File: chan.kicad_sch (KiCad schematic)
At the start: 8 parts, among them J5 0836149012, J6 61083-061402LF, J7 61083-061402LF

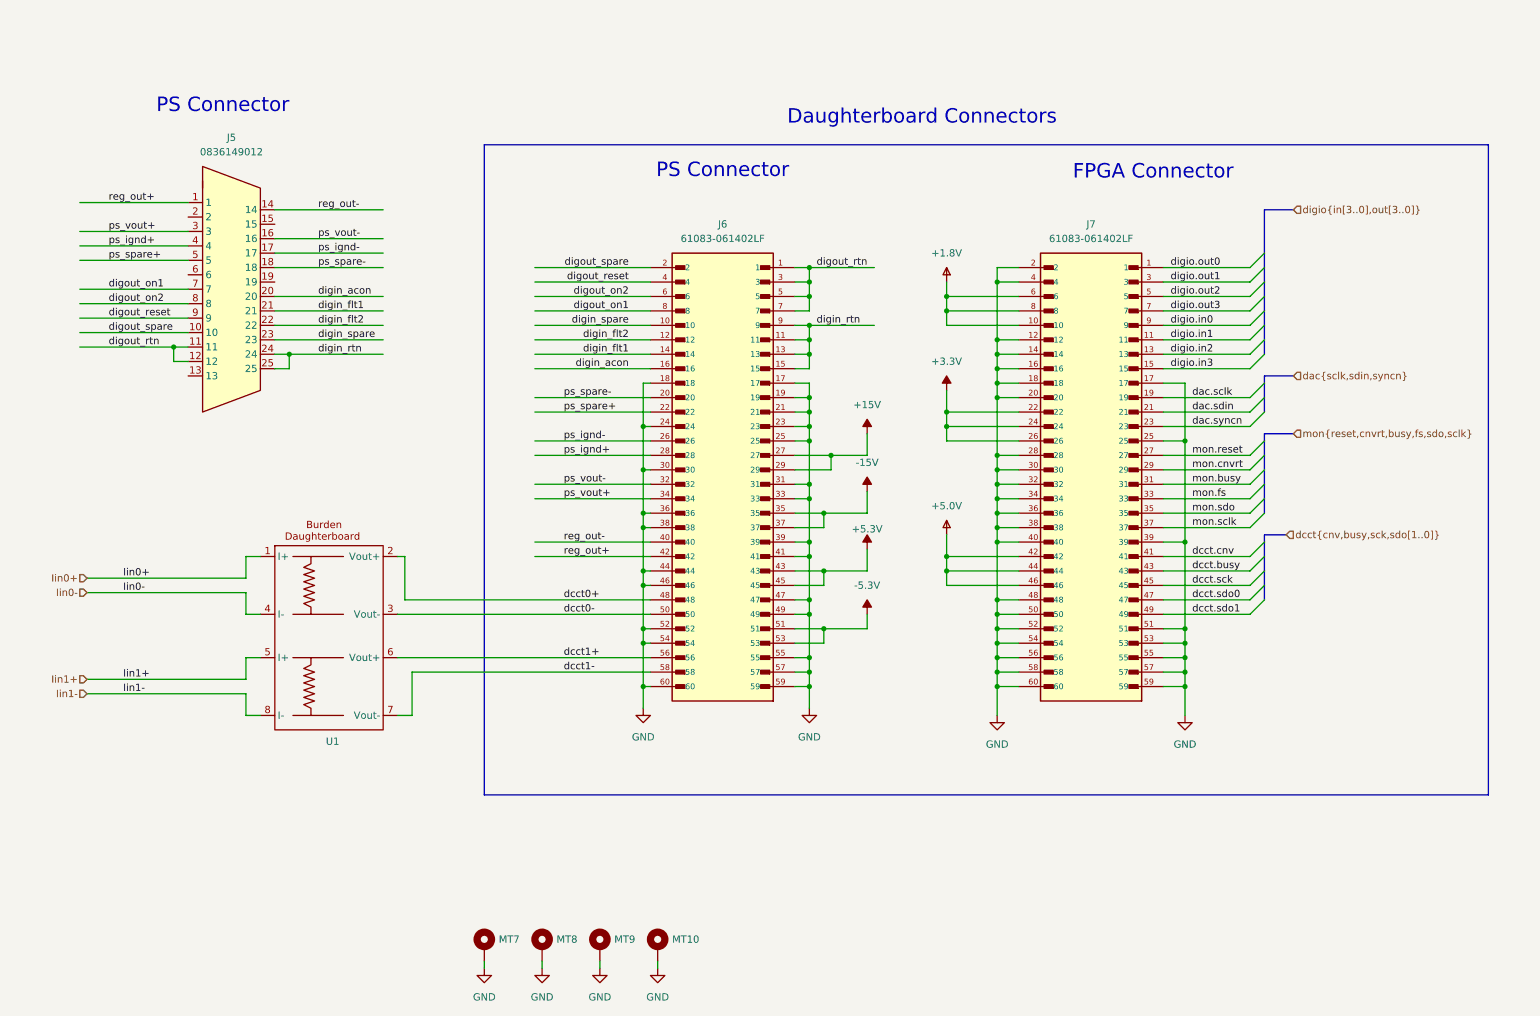
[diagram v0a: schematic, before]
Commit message: Add all 4 channels
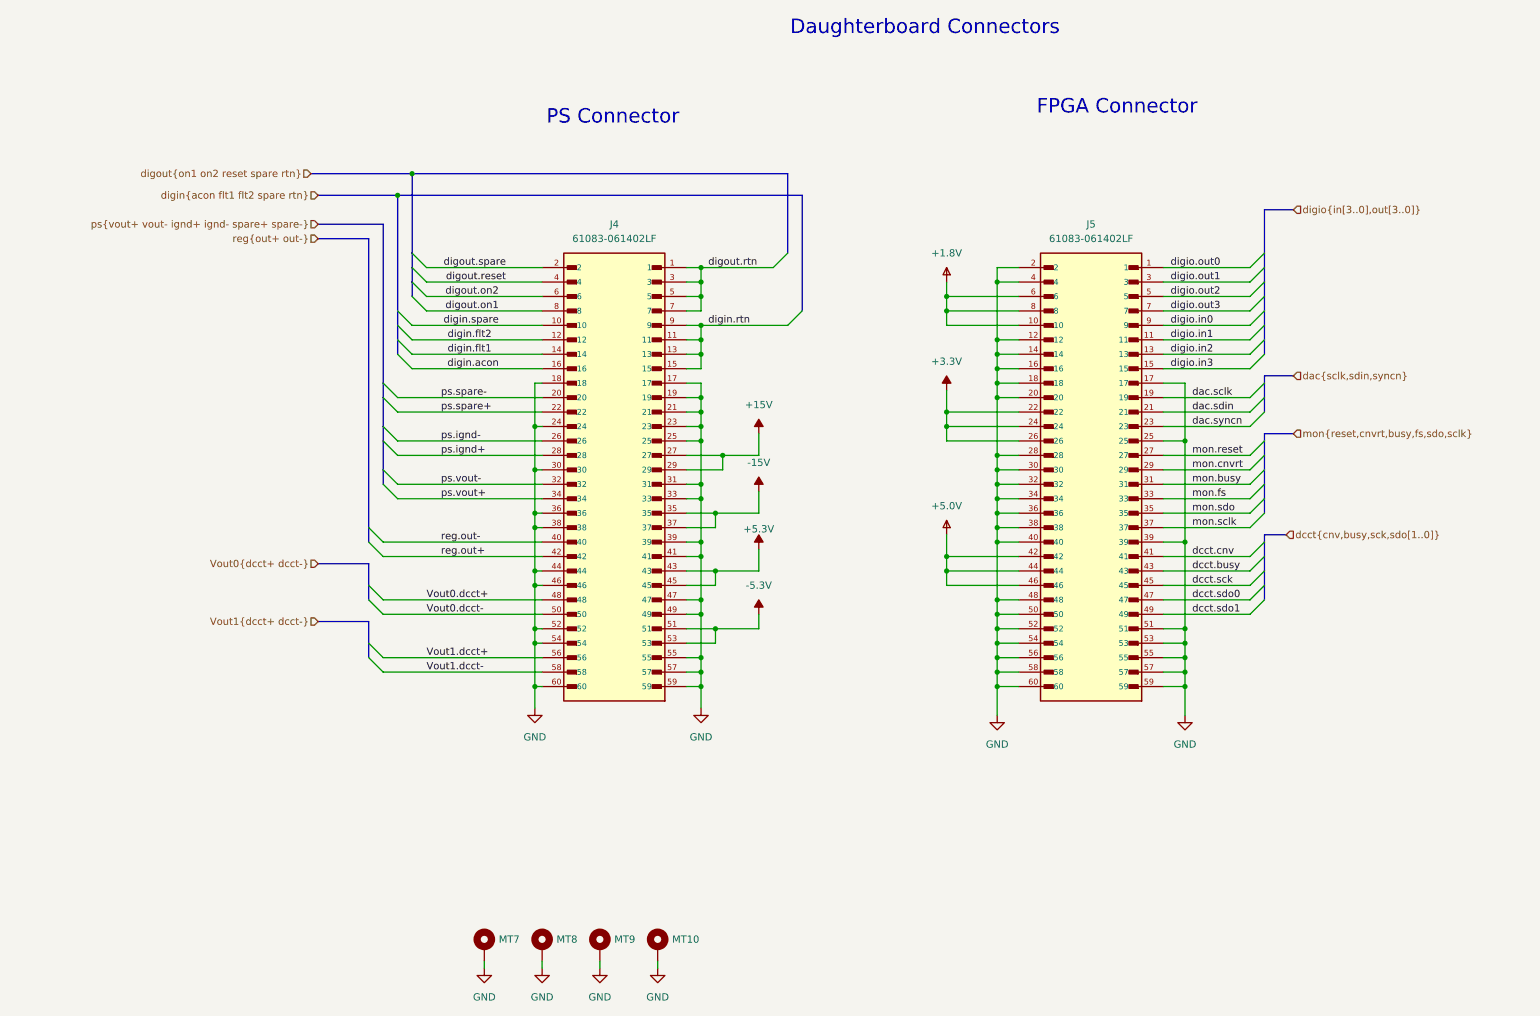
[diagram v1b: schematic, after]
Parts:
- removed J5: 0836149012, myparts:0836149012, symbol 0836149012:0836149012
- removed U1: ~, myparts:burden, symbol psc:burden
- renumbered J6 to J4, J7 to J5
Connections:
- net dcct0+ renamed Vout0.dcct+
- net dcct0- renamed Vout0.dcct-
- net dcct1+ renamed Vout1.dcct+
- net dcct1- renamed Vout1.dcct-
- net digin_acon renamed digin.acon
- net digin_flt1 renamed digin.flt1
- net digin_flt2 renamed digin.flt2
- net digin_rtn renamed digin.rtn
- net digin_spare renamed digin.spare
- net digout_on1 renamed digout.on1
- net digout_on2 renamed digout.on2
- net digout_reset renamed digout.reset
- net digout_rtn renamed digout.rtn
- net digout_spare renamed digout.spare
- net ps_ignd+ renamed ps.ignd+
- net ps_ignd- renamed ps.ignd-
- net ps_spare+ renamed ps.spare+
- net ps_spare- renamed ps.spare-
- net ps_vout+ renamed ps.vout+
- net ps_vout- renamed ps.vout-
- net reg_out+ renamed reg.out+
- net reg_out- renamed reg.out-
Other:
- moved on the sheet: J4

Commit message: Start routing
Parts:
- renumbered J4 to J5, J5 to J6
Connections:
- net digin.rtn: now also J5.1, J5.3, J5.5, J5.7; no longer J5.11, J5.13, J5.15, J5.9
- net digout.rtn: now also J5.11, J5.13, J5.15, J5.9; no longer J5.1, J5.3, J5.5, J5.7

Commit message: Finished layout
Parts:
- J5, J6: Cost (none) -> 2.81; MFG (none) -> Amphenol; MFG_PN (none) -> 61083-061402LF
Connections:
- net GND: no longer J6.56, J6.58, J6.60
- new net +2.5V: J6.56, J6.58, J6.60
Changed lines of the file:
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@@
 	)
 	(junction
-		(at 179.07 86.36)
+		(at 179.07 132.08)
 		(diameter 0)
 		(color 0 0 0 0)
 	)
 	(junction
-		(at 179.07 111.76)
+		(at 179.07 86.36)
 		(diameter 0)
 		(color 0 0 0 0)
 	)
 	(junction
-		(at 220.98 109.22)
+		(at 179.07 111.76)
 		(diameter 0)
 		(color 0 0 0 0)
 	)
 	(junction
-		(at 187.96 127)
+		(at 220.98 109.22)
 		(diameter 0)
 		(color 0 0 0 0)
 	)
 	(junction
-		(at 187.96 132.08)
+		(at 187.96 127)
 		(diameter 0)
 		(color 0 0 0 0)
@@
 	)
 	(junction
-		(at 187.96 134.62)
-		(diameter 0)
-		(color 0 0 0 0)
-	)
-	(junction
 		(at 179.07 68.58)
 		(diameter 0)
@@
 	)
 	(junction
-		(at 187.96 129.54)
-		(diameter 0)
-		(color 0 0 0 0)
-	)
-	(junction
 		(at 138.43 104.14)
 		(diameter 0)
@@
 	)
 	(junction
+		(at 179.07 129.54)
+		(diameter 0)
+		(color 0 0 0 0)
+	)
+	(junction
 		(at 135.89 66.04)
 		(diameter 0)
@@
 	(wire
 		(pts
+			(xy 179.07 129.54) (xy 179.07 127)
+		)
+		(stroke
+			(width 0)
+			(type default)
+		)
+	)
+	(wire
+		(pts
 			(xy 135.89 88.9) (xy 135.89 91.44)
 		)
@@
 	(wire
 		(pts
-			(xy 187.96 134.62) (xy 187.96 139.7)
+			(xy 187.96 127) (xy 187.96 139.7)
 		)
 		(stroke
@@
 	(wire
 		(pts
-			(xy 187.96 129.54) (xy 187.96 132.08)
-		)
-		(stroke
-			(width 0)
-			(type default)
-		)
-	)
-	(wire
-		(pts
 			(xy 133.35 91.44) (xy 135.89 91.44)
 		)
@@
 		)
 	)
-	(wire
-		(pts
-			(xy 191.77 134.62) (xy 187.96 134.62)
-		)
-		(stroke
-			(width 0)
-			(type default)
-		)
-	)
 	(bus
 		(pts
@@
 	(wire
 		(pts
-			(xy 191.77 129.54) (xy 187.96 129.54)
-		)
-		(stroke
-			(width 0)
-			(type default)
-		)
-	)
-	(wire
-		(pts
 			(xy 187.96 93.98) (xy 187.96 96.52)
 		)
@@
 		)
 	)
-	(wire
-		(pts
-			(xy 191.77 132.08) (xy 187.96 132.08)
-		)
-		(stroke
-			(width 0)
-			(type default)
-		)
-	)
 	(bus
 		(pts
@@
 	(wire
 		(pts
+			(xy 191.77 129.54) (xy 179.07 129.54)
+		)
+		(stroke
+			(width 0)
+			(type default)
+		)
+	)
+	(wire
+		(pts
 			(xy 97.79 184.15) (xy 97.79 182.88)
 		)
@@
 	(wire
 		(pts
-			(xy 187.96 132.08) (xy 187.96 134.62)
-		)
-		(stroke
-			(width 0)
-			(type default)
-		)
-	)
-	(wire
-		(pts
 			(xy 133.35 99.06) (xy 135.89 99.06)
 		)
@@
 		)
 	)
+	(wire
+		(pts
+			(xy 179.07 134.62) (xy 179.07 132.08)
+		)
+		(stroke
+			(width 0)
+			(type default)
+		)
+	)
 	(bus
 		(pts
@@
 	(wire
 		(pts
+			(xy 179.07 132.08) (xy 179.07 129.54)
+		)
+		(stroke
+			(width 0)
+			(type default)
+		)
+	)
+	(wire
+		(pts
 			(xy 191.77 119.38) (xy 187.96 119.38)
 		)
@@
 	(wire
 		(pts
+			(xy 191.77 132.08) (xy 179.07 132.08)
+		)
+		(stroke
+			(width 0)
+			(type default)
+		)
+	)
+	(wire
+		(pts
 			(xy 179.07 63.5) (xy 179.07 66.04)
 		)
@@
 	(wire
 		(pts
-			(xy 106.68 124.46) (xy 106.68 127)
+			(xy 191.77 134.62) (xy 179.07 134.62)
 		)
 		(stroke
@@
 	(wire
 		(pts
-			(xy 191.77 121.92) (xy 187.96 121.92)
+			(xy 106.68 124.46) (xy 106.68 127)
 		)
 		(stroke
@@
 	(wire
 		(pts
-			(xy 191.77 66.04) (xy 179.07 66.04)
+			(xy 191.77 121.92) (xy 187.96 121.92)
 		)
 		(stroke
@@
 	(wire
 		(pts
-			(xy 135.89 101.6) (xy 135.89 109.22)
+			(xy 191.77 66.04) (xy 179.07 66.04)
 		)
 		(stroke
@@
 	(wire
 		(pts
-			(xy 133.35 119.38) (xy 135.89 119.38)
+			(xy 135.89 101.6) (xy 135.89 109.22)
 		)
 		(stroke
@@
 	(wire
 		(pts
-			(xy 187.96 127) (xy 187.96 129.54)
+			(xy 133.35 119.38) (xy 135.89 119.38)
 		)
 		(stroke
@@
 	)
 	(symbol
+		(lib_id "psc:+2.5V")
+		(at 179.07 127 0)
+		(unit 1)
+		(exclude_from_sim no)
+		(in_bom yes)
+		(on_board yes)
+		(dnp no)
+		(fields_autoplaced yes)
+		(property "Reference" "#PWR0232"
+			(at 179.07 130.81 0)
+			(effects
+				(font
+					(size 1.27 1.27)
+				)
+				(hide yes)
+			)
+		)
+		(property "Value" "+2.5V"
+			(at 179.07 121.92 0)
+			(effects
+				(font
+					(size 1.27 1.27)
+				)
+			)
+		)
+		(property "Footprint" ""
+			(at 179.07 127 0)
+			(effects
+				(font
+					(size 1.27 1.27)
+				)
+				(hide yes)
+			)
+		)
+		(property "Datasheet" ""
+			(at 179.07 127 0)
+			(effects
+				(font
+					(size 1.27 1.27)
+				)
+				(hide yes)
+			)
+		)
+		(property "Description" "Power symbol creates a global label with name \"-15V\""
+			(at 179.07 127 0)
+			(effects
+				(font
+					(size 1.27 1.27)
+				)
+				(hide yes)
+			)
+		)
+		(pin "1"
+		)
+		(instances
+			(project ""
+				(path "/40891cc8-bf64-41f4-8f69-a607d7b280eb/66704ae2-4e31-439d-ae4e-acdb607106a4"
+					(reference "#PWR0234")
+					(unit 1)
+				)
+				(path "/40891cc8-bf64-41f4-8f69-a607d7b280eb/68fa8dde-6b87-4418-ab24-6dd6792cf3f7"
+					(reference "#PWR0232")
+					(unit 1)
+				)
+				(path "/40891cc8-bf64-41f4-8f69-a607d7b280eb/79ccc009-8b32-4834-80e8-facad3ab4620"
+					(reference "#PWR0233")
+					(unit 1)
+				)
+				(path "/40891cc8-bf64-41f4-8f69-a607d7b280eb/bff48835-53bb-47a9-9e6c-9af939cbdeca"
+					(reference "#PWR0235")
+					(unit 1)
+				)
+			)
+		)
+	)
+	(symbol
 		(lib_id "power:GND")
 		(at 135.89 138.43 0)
@@
 			)
 		)
-		(property "Description" ""
+		(property "Description" "CONN PLUG 60POS SMD GOLD"
 			(at 120.65 96.52 0)
 			(effects
@@
 			)
 		)
+		(property "Cost" "2.81"
+			(at 120.65 96.52 0)
+			(effects
+				(font
+					(size 1.27 1.27)
+				)
+				(hide yes)
+			)
+		)
+		(property "MFG" "Amphenol"
+			(at 120.65 96.52 0)
+			(effects
+				(font
+					(size 1.27 1.27)
+				)
+				(hide yes)
+			)
+		)
+		(property "MFG_PN" "61083-061402LF"
+			(at 120.65 96.52 0)
+			(effects
+				(font
+					(size 1.27 1.27)
+				)
+				(hide yes)
+			)
+		)
 		(pin "48"
 		)
@@
 			)
 		)
-		(property "Description" ""
+		(property "Description" "CONN PLUG 60POS SMD GOLD"
 			(at 204.47 96.52 0)
 			(effects
@@
 				(hide yes)
 			)
+		)
+		(property "Cost" "2.81"
+			(at 204.47 96.52 0)
+			(effects
+				(font
+					(size 1.27 1.27)
+				)
+				(hide yes)
+			)
+		)
+		(property "MFG" "Amphenol"
+			(at 204.47 96.52 0)
+			(effects
+				(font
+					(size 1.27 1.27)
+				)
+				(hide yes)
+			)
+		)
+		(property "MFG_PN" "61083-061402LF"
+			(at 204.47 96.52 0)
+			(effects
+				(font
+					(size 1.27 1.27)
+				)
+				(hide yes)
+			)
